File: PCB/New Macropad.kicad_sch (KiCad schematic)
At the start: 14 parts, among them J1 Conn_01x04_Pin, SW1 SW_Push, SW2 SW_Push, SW3 SW_Push, SW4 SW_Push, SW5 SW_Push, SW6 SW_Push, U1 XIAO-RP2040-DIP

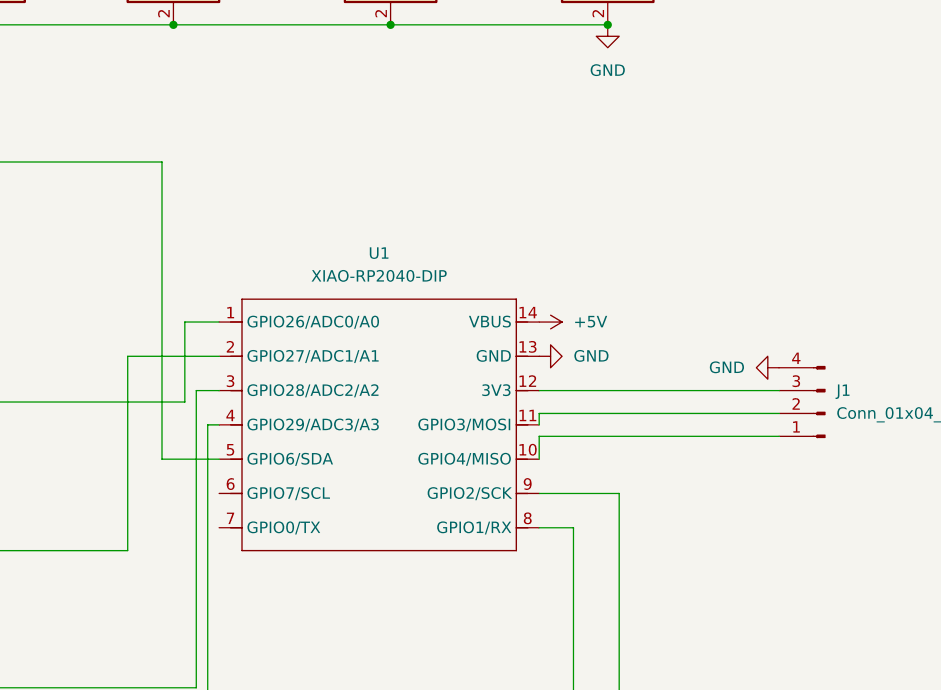
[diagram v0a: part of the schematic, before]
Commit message: Changed PCB OLED wiring
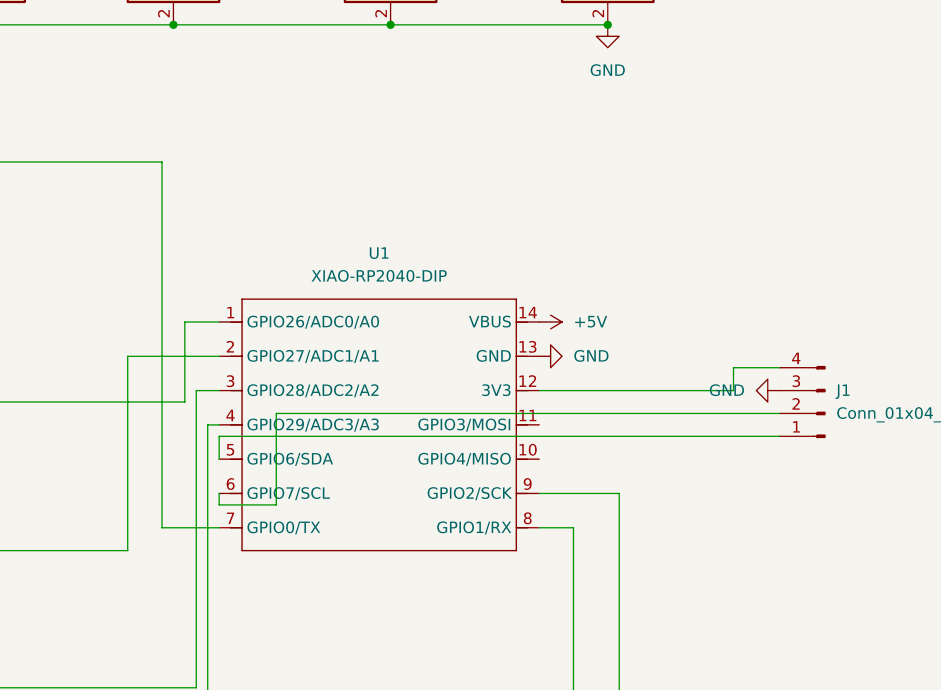
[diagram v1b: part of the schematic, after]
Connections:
- net GND: now also J1.3 (Pin_3); no longer J1.4 (Pin_4)
- net at J1.1 (Pin_1): now also U1.5 (GPIO6/SDA); no longer U1.10 (GPIO4/MISO)
- net at J1.2 (Pin_2): now also U1.6 (GPIO7/SCL); no longer U1.11 (GPIO3/MOSI)
- net at U1.12 (3V3): now also J1.4 (Pin_4); no longer J1.3 (Pin_3)
- net at D1.3 (DIN): now also U1.7 (GPIO0/TX); no longer U1.5 (GPIO6/SDA)
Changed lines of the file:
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@@
-	(wire
-		(pts
-			(xy 191.77 90.17) (xy 165.1 90.17)
-		)
-		(stroke
-			(width 0)
-			(type default)
-		)
-	)
 	(wire
 		(pts
@@
 	(wire
 		(pts
+			(xy 186.69 85.09) (xy 191.77 85.09)
+		)
+		(stroke
+			(width 0)
+			(type default)
+		)
+	)
+	(wire
+		(pts
 			(xy 156.21 39.37) (xy 165.1 39.37)
 		)
@@
 	(wire
 		(pts
+			(xy 186.69 87.63) (xy 186.69 85.09)
+		)
+		(stroke
+			(width 0)
+			(type default)
+		)
+	)
+	(wire
+		(pts
 			(xy 125.73 88.9) (xy 125.73 80.01)
 		)
@@
 	(wire
 		(pts
-			(xy 123.19 62.23) (xy 123.19 95.25)
-		)
-		(stroke
-			(width 0)
-			(type default)
-		)
-	)
-	(wire
-		(pts
 			(xy 102.87 46.99) (xy 124.46 46.99)
 		)
@@
 	(wire
 		(pts
+			(xy 129.54 92.71) (xy 129.54 95.25)
+		)
+		(stroke
+			(width 0)
+			(type default)
+		)
+	)
+	(wire
+		(pts
+			(xy 191.77 92.71) (xy 129.54 92.71)
+		)
+		(stroke
+			(width 0)
+			(type default)
+		)
+	)
+	(wire
+		(pts
 			(xy 173.99 172.72) (xy 173.99 99.06)
 		)
@@
 	(wire
 		(pts
-			(xy 165.1 87.63) (xy 191.77 87.63)
-		)
-		(stroke
-			(width 0)
-			(type default)
-		)
-	)
-	(wire
-		(pts
 			(xy 54.61 88.9) (xy 54.61 105.41)
 		)
@@
 	(wire
 		(pts
+			(xy 129.54 100.33) (xy 129.54 99.06)
+		)
+		(stroke
+			(width 0)
+			(type default)
+		)
+	)
+	(wire
+		(pts
 			(xy 102.87 31.75) (xy 124.46 31.75)
 		)
@@
 	(wire
 		(pts
+			(xy 135.89 90.17) (xy 191.77 90.17)
+		)
+		(stroke
+			(width 0)
+			(type default)
+		)
+	)
+	(wire
+		(pts
 			(xy 64.77 172.72) (xy 173.99 172.72)
 		)
@@
 	(wire
 		(pts
-			(xy 191.77 92.71) (xy 165.1 92.71)
+			(xy 123.19 62.23) (xy 123.19 102.87)
 		)
 		(stroke
@@
 	(wire
 		(pts
-			(xy 165.1 90.17) (xy 165.1 91.44)
-		)
-		(stroke
-			(width 0)
-			(type default)
-		)
-	)
-	(wire
-		(pts
 			(xy 173.99 99.06) (xy 165.1 99.06)
 		)
@@
 	(wire
 		(pts
+			(xy 135.89 90.17) (xy 135.89 100.33)
+		)
+		(stroke
+			(width 0)
+			(type default)
+		)
+	)
+	(wire
+		(pts
 			(xy 168.91 156.21) (xy 168.91 102.87)
 		)
@@
 	(wire
 		(pts
-			(xy 165.1 92.71) (xy 165.1 95.25)
-		)
-		(stroke
-			(width 0)
-			(type default)
-		)
-	)
-	(wire
-		(pts
 			(xy 81.28 46.99) (xy 102.87 46.99)
 		)
@@
 	(wire
 		(pts
-			(xy 123.19 95.25) (xy 129.54 95.25)
-		)
-		(stroke
-			(width 0)
-			(type default)
-		)
-	)
-	(wire
-		(pts
 			(xy 110.49 39.37) (xy 116.84 39.37)
 		)
@@
 	(wire
 		(pts
+			(xy 123.19 102.87) (xy 129.54 102.87)
+		)
+		(stroke
+			(width 0)
+			(type default)
+		)
+	)
+	(wire
+		(pts
 			(xy 54.61 156.21) (xy 54.61 172.72)
 		)
@@
 	(wire
 		(pts
+			(xy 165.1 87.63) (xy 186.69 87.63)
+		)
+		(stroke
+			(width 0)
+			(type default)
+		)
+	)
+	(wire
+		(pts
 			(xy 60.96 31.75) (xy 81.28 31.75)
 		)
@@
 		(pts
 			(xy 128.27 91.44) (xy 129.54 91.44)
+		)
+		(stroke
+			(width 0)
+			(type default)
+		)
+	)
+	(wire
+		(pts
+			(xy 135.89 100.33) (xy 129.54 100.33)
 		)
 		(stroke
@@
 	(symbol
 		(lib_id "power:GND")
-		(at 191.77 85.09 270)
+		(at 191.77 87.63 270)
 		(unit 1)
 		(exclude_from_sim no)
@@
 		(fields_autoplaced yes)
 		(property "Reference" "#PWR06"
-			(at 185.42 85.09 0)
+			(at 185.42 87.63 0)
 			(effects
 				(font
@@
 		)
 		(property "Value" "GND"
-			(at 187.96 85.0899 90)
+			(at 187.96 87.6299 90)
 			(effects
 				(font
@@
 		)
 		(property "Footprint" ""
-			(at 191.77 85.09 0)
+			(at 191.77 87.63 0)
 			(effects
 				(font
@@
 		)
 		(property "Datasheet" ""
-			(at 191.77 85.09 0)
+			(at 191.77 87.63 0)
 			(effects
 				(font
@@
 		)
 		(property "Description" "Power symbol creates a global label with name \"GND\" , ground"
-			(at 191.77 85.09 0)
-			(effects
-				(font
+			(at 191.77 87.63 0)
+			(effects
+				(font
